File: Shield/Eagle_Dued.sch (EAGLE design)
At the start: 76 parts, among them IC1 7805TV, IC2 LM340MP-05

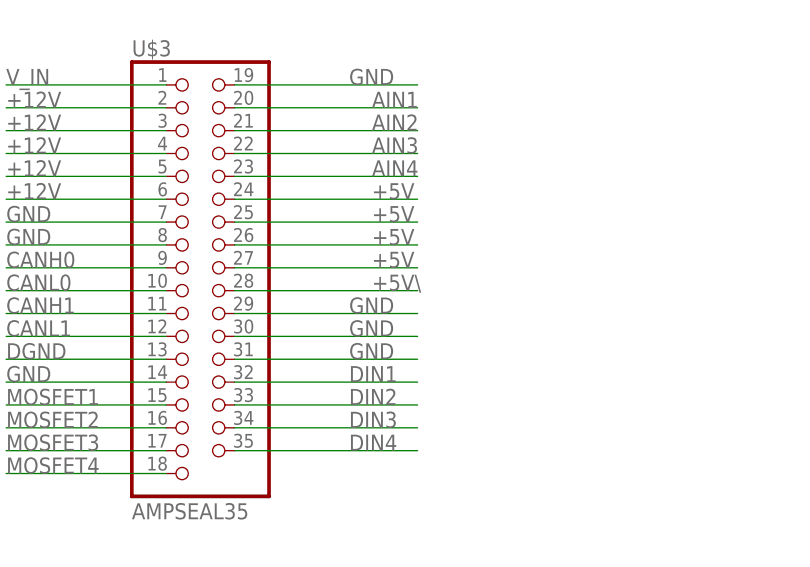
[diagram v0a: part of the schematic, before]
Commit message: Newer version of analog board, new version of DueD
Dued board now properly sized for the new case.
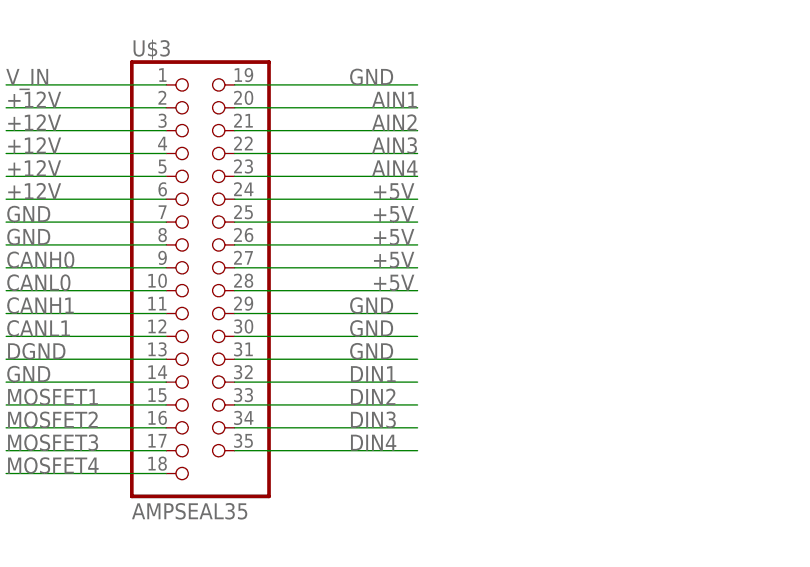
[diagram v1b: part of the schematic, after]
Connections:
- removed net +5V\: U$3.28
- net +5V: now also U$3.28
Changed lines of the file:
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@@
 <pinref part="U$3" gate="G$1" pin="27"/>
+</segment>
+<segment>
+<wire x1="551.18" y1="144.78" x2="571.5" y2="144.78" width="0.1524" layer="91"/>
+<label x="566.42" y="144.78" size="1.778" layer="95"/>
+<pinref part="U$3" gate="G$1" pin="28"/>
 </segment>
 </net>
@@
 </segment>
 </net>
-<net name="+5V\" class="0">
-<segment>
-<wire x1="551.18" y1="144.78" x2="571.5" y2="144.78" width="0.1524" layer="91"/>
-<label x="566.42" y="144.78" size="1.778" layer="95"/>
-<pinref part="U$3" gate="G$1" pin="28"/>
-</segment>
-</net>
